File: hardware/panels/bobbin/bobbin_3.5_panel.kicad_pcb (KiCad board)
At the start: 2 copper layers, 78.5 x 105 mm, 34 parts

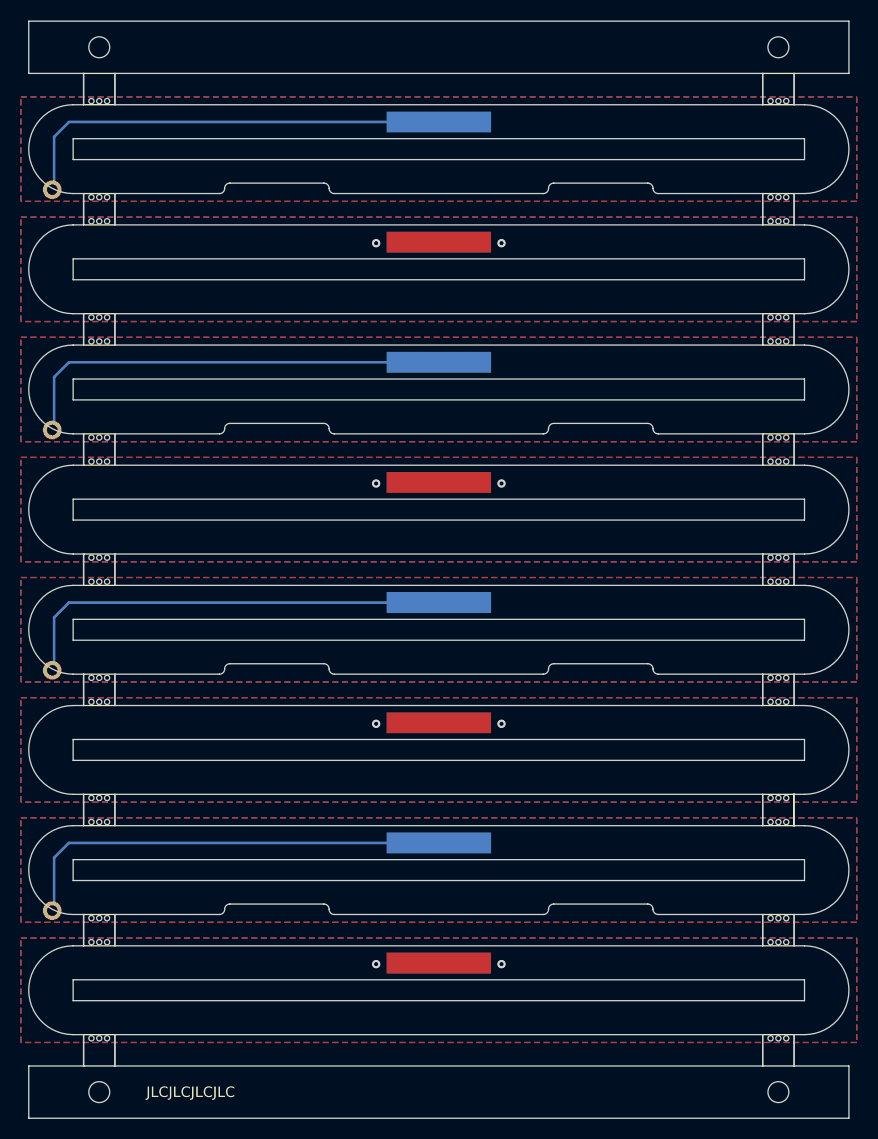
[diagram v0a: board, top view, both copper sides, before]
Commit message: Preamp, Tone Block, Passive, and Bobbin Panel updates
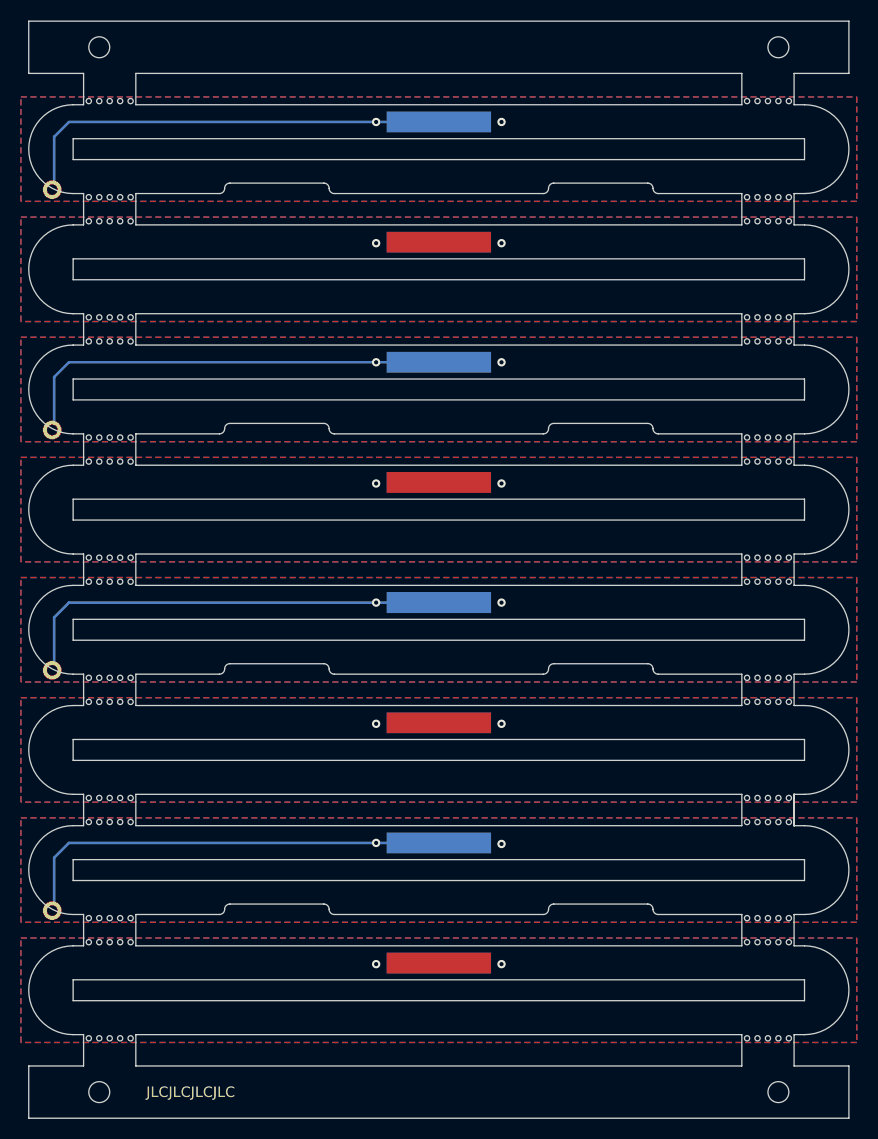
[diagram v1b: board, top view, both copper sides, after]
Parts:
- moved mouse-bite-3mm-slot 1.00 mm to (121.5, 141.5)
- moved mouse-bite-3mm-slot 1.00 mm to (58.5, 84.0)
- moved mouse-bite-3mm-slot 1.00 mm to (121.5, 118.5)
- moved mouse-bite-3mm-slot 1.00 mm to (121.5, 95.5)
- moved mouse-bite-3mm-slot 1.00 mm to (58.5, 118.5)
- moved mouse-bite-3mm-slot 1.00 mm to (58.5, 95.5)
- moved mouse-bite-3mm-slot 1.00 mm to (58.5, 72.5)
- moved mouse-bite-3mm-slot 1.00 mm to (121.5, 72.5)
- moved mouse-bite-3mm-slot 1.00 mm to (121.5, 61.0)
- moved mouse-bite-3mm-slot 1.00 mm to (58.5, 61.0)
- moved mouse-bite-3mm-slot 1.00 mm to (58.5, 141.5)
- moved mouse-bite-3mm-slot 1.00 mm to (121.5, 49.5)
- moved mouse-bite-3mm-slot 1.00 mm to (58.5, 49.5)
- moved mouse-bite-3mm-slot 1.00 mm to (121.5, 130.0)
- moved mouse-bite-3mm-slot 1.00 mm to (121.5, 107.0)
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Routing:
- net GND: vias 8 -> 16
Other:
- outline, holes or cut-outs redrawn
